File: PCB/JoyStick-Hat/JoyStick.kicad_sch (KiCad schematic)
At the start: 14 parts, among them J14 Conn_01x03_Pin, J15 Conn_01x03_Pin, J4 Conn_02x04_Odd_Even, J8 Conn_02x04_Odd_Even

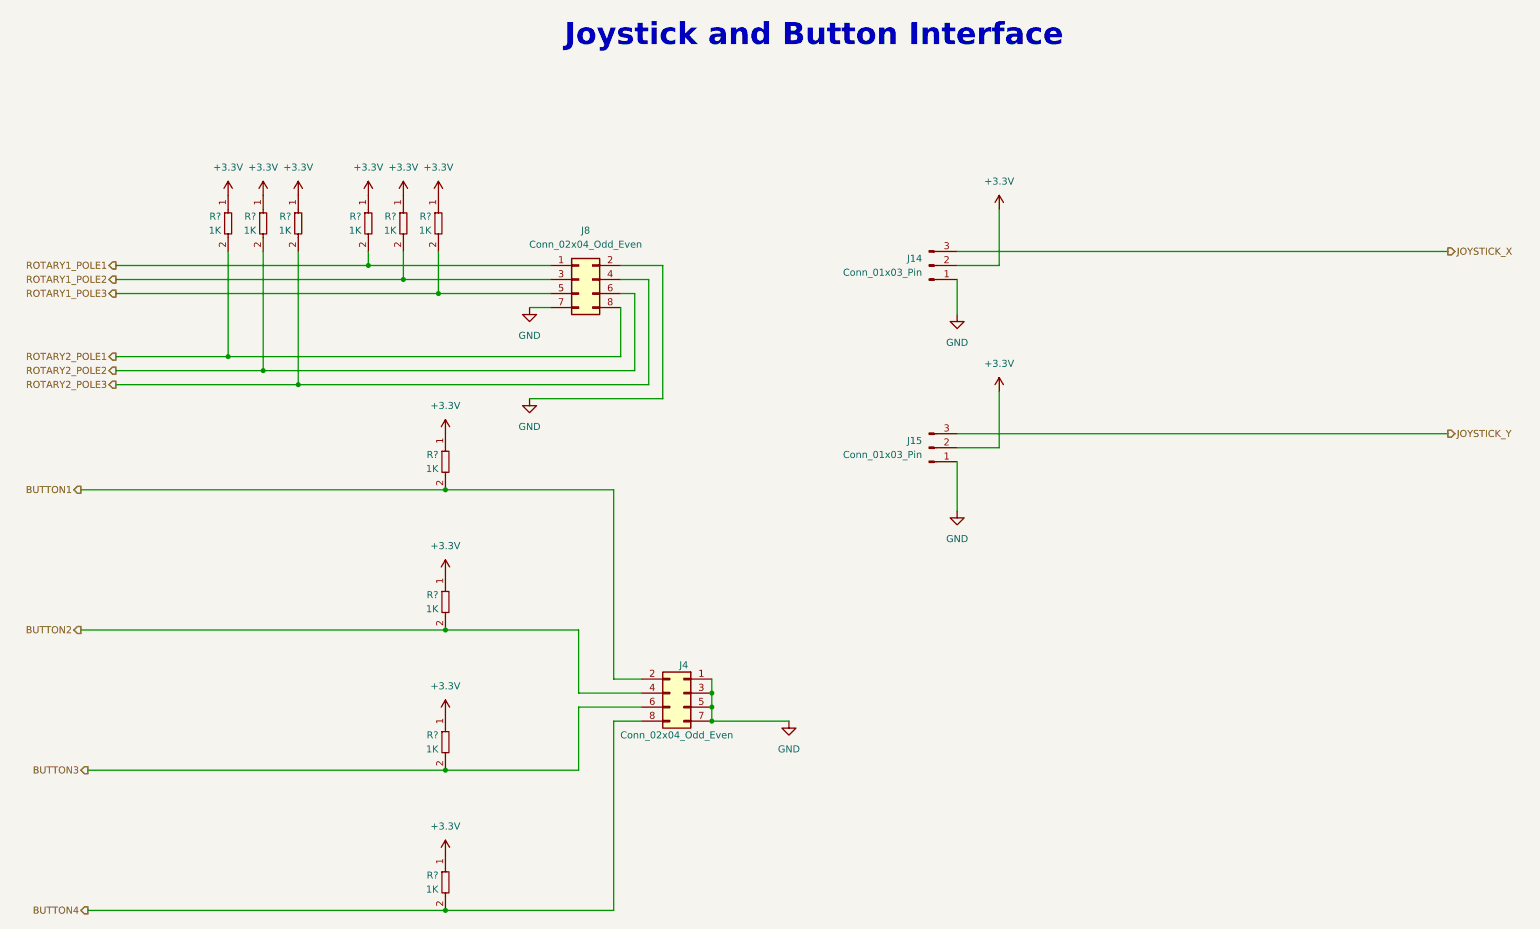
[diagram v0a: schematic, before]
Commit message: James Fixes and 3D models
Added all the changes that James suggested to the design and then added 3D models to the board for mechanical design purposes. Generated 3D renders of the board and added them to new directory called img.
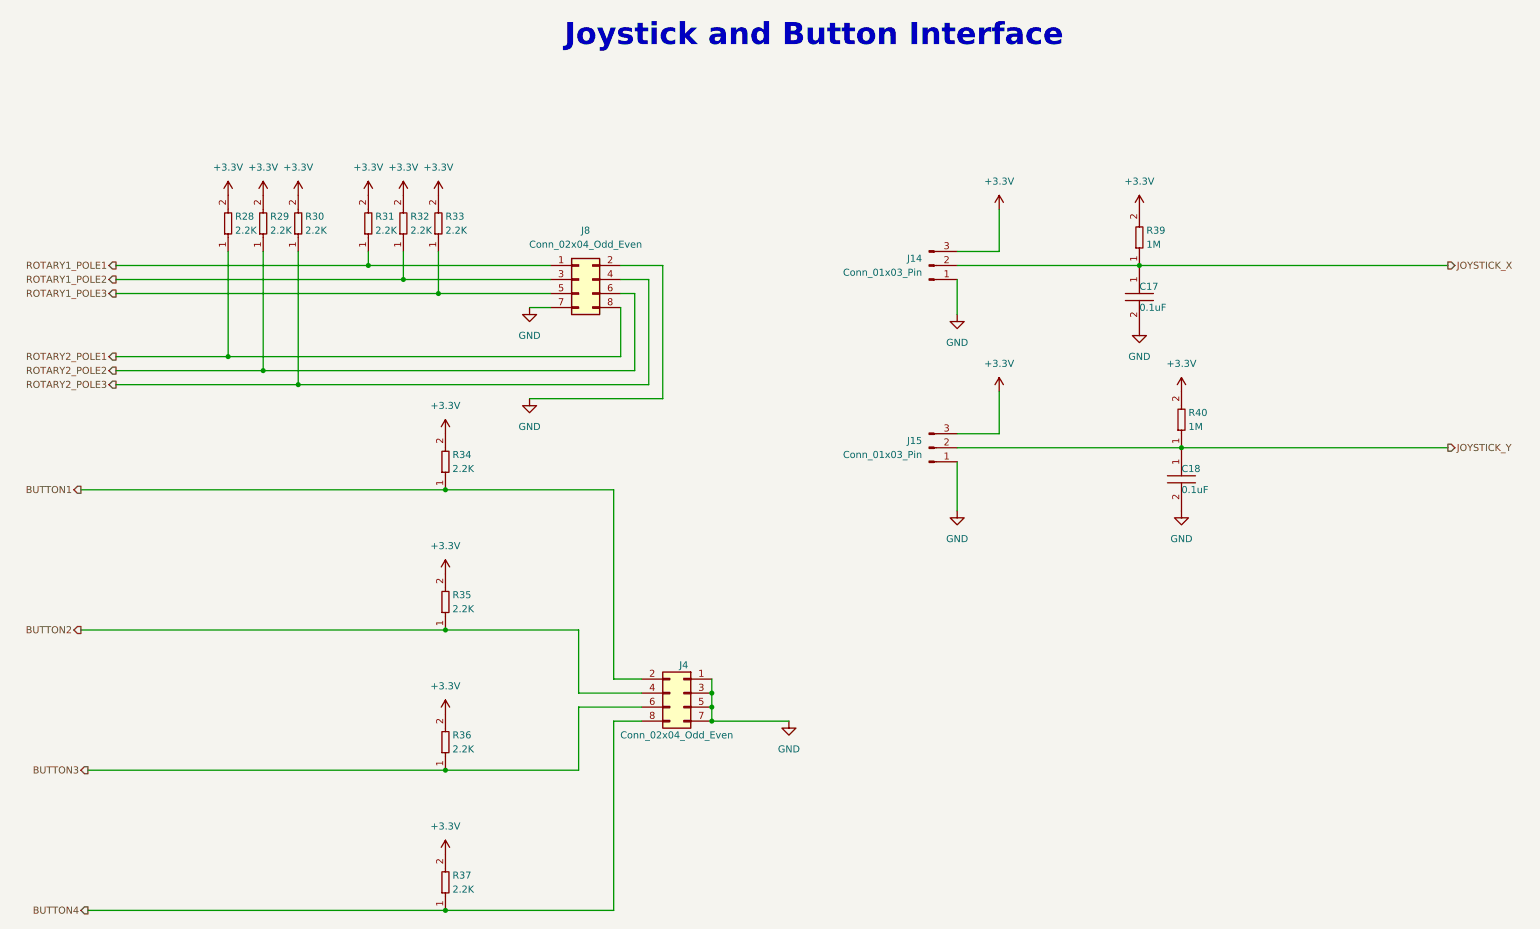
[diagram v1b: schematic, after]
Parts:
- removed R? (x10): RC0402FR-071KL, AVR-KiCAD-Lib-Resistors:R0402, symbol AVR-KiCAD-Lib-Resistors:RC0402FR-071KL
- added C17, C18: C0402C104K9PACTU, AVR-KiCAD-Lib-Resistors:R0402, symbol AVR-KiCAD-Lib-Capacitors:C0402C104K9PACTU
- added R28, R29, R30, R31, R32, R33, R34, R35, R36, R37: RC0402FR-072K2L, AVR-KiCAD-Lib-Resistors:R0402, symbol AVR-KiCAD-Lib-Resistors:RC0402FR-072K2L
- added R39, R40: RT0603BRD071ML, AVR-KiCAD-Lib-Resistors:R0603, symbol AVR-KiCAD-Lib-Resistors:RT0603BRD071ML
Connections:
- net +3.3V: now also J14.3 (Pin_3), J15.3 (Pin_3), R28.2, R29.2, R30.2, R31.2, R32.2, R33.2, R34.2, R35.2, R36.2, R37.2, R39.2, R40.2; no longer J14.2 (Pin_2), J15.2 (Pin_2)
- net BUTTON1: now also R34.1
- net BUTTON2: now also R35.1
- net BUTTON3: now also R36.1
- net BUTTON4: now also R37.1
- net GND: now also C17.2, C18.2
- net JOYSTICK_X: now also J14.2 (Pin_2), C17.1, R39.1; no longer J14.3 (Pin_3)
- net JOYSTICK_Y: now also J15.2 (Pin_2), C18.1, R40.1; no longer J15.3 (Pin_3)
- net ROTARY1_POLE1: now also R31.1
- net ROTARY1_POLE2: now also R32.1
- net ROTARY1_POLE3: now also R33.1
- net ROTARY2_POLE1: now also R28.1
- net ROTARY2_POLE2: now also R29.1
- net ROTARY2_POLE3: now also R30.1
